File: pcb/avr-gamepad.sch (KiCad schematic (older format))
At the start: 64 parts, among them J1 Conn_01x06, J2 Conn_01x06, J3 Conn_01x05, J4 Conn_01x05, P1 USB_C_Plug_USB2.0, SW1 RESET, SW10 R2, SW11 A, SW13 Left, SW14 L2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

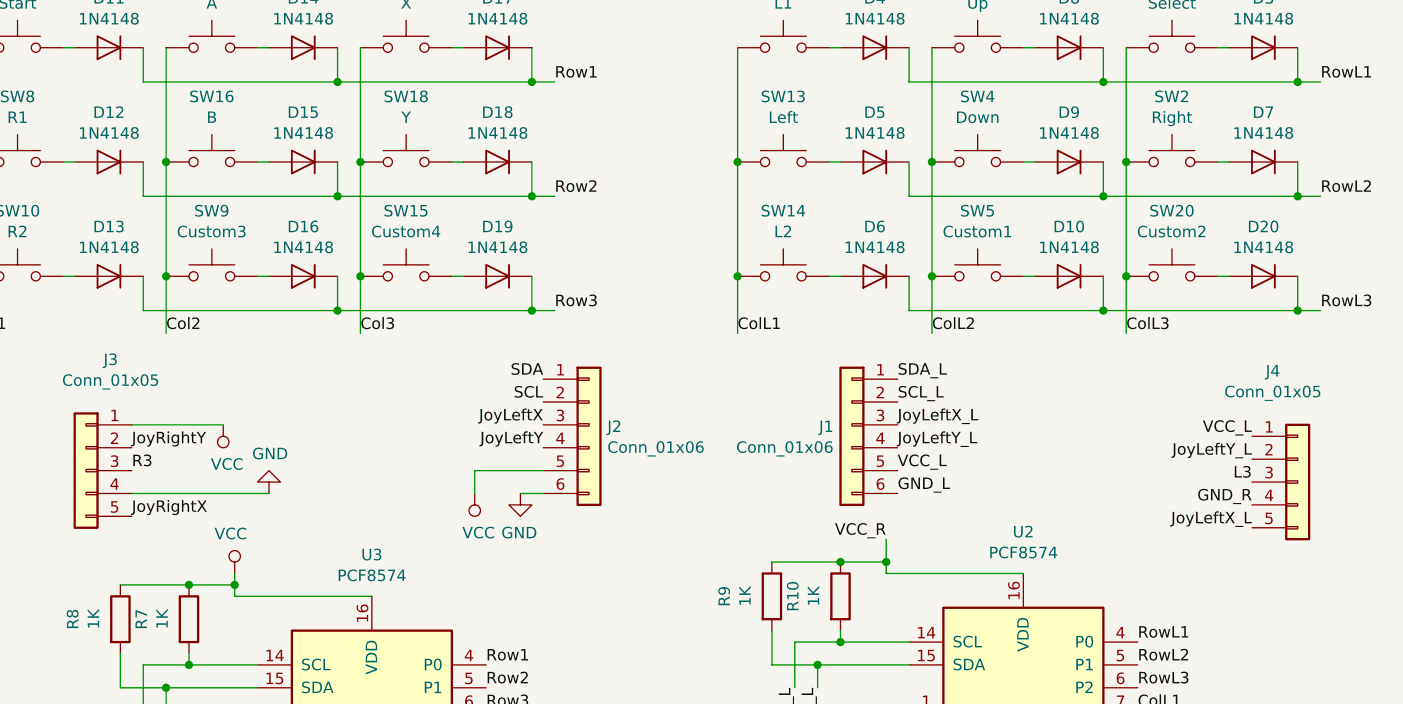
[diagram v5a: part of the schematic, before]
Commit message: disabled extra buttons, fixed R-L conversion
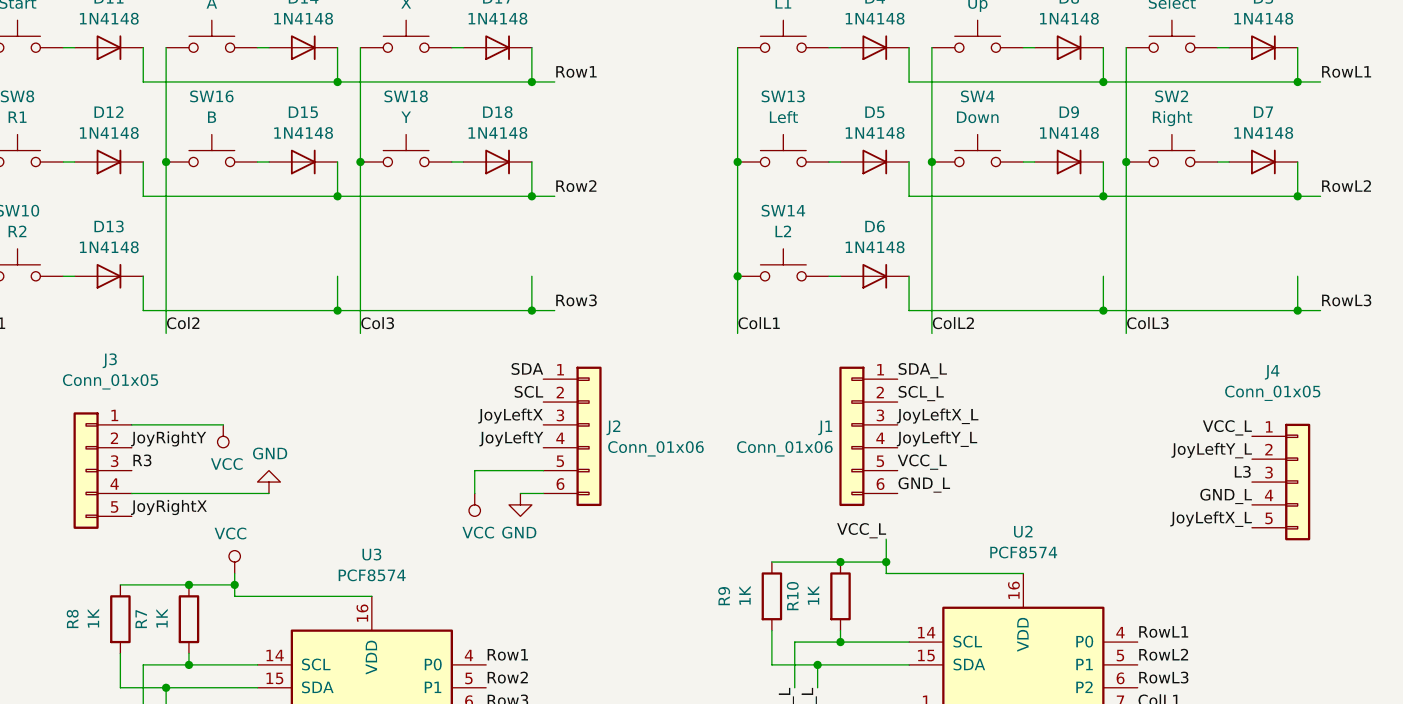
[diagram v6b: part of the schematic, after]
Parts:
- removed D10, D16, D19, D20: 1N4148, Diode_SMD:D_0603_1608Metric, symbol Diode:1N4148
- removed SW15: Custom4, button-contacts:Small, symbol Switch:SW_Push
- removed SW20: Custom2, button-contacts:Small, symbol Switch:SW_Push
- removed SW5: Custom1, button-contacts:Large_tapered, symbol Switch:SW_Push
- removed SW9: Custom3, button-contacts:Small, symbol Switch:SW_Push
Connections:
- net GND_R is gone; now on net GND_L: J4.4 (Pin_4)
- net VCC_R is gone; now on net VCC_L: R10.1, R9.1, U2.16 (VDD)
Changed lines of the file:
@@
 EESchema Schematic File Version 4
-LIBS:avr-gamepad-cache
-EELAYER 29 0
+EELAYER 30 0
 EELAYER END
 $Descr A4 11693 8268
@@
 GND_L
 Text Label 10500 2900 2    50   ~ 0
-GND_R
+GND_L
 Text Label 5600 2950 0    50   ~ 0
 JoyRightX
@@
 Wire Wire Line
 	8250 900  8250 1400
-Wire Wire Line
-	9100 1400 9100 1900
 Connection ~ 9100 1400
 Wire Wire Line
 	9100 900  9100 1400
-Wire Wire Line
-	9950 1400 9950 1900
 Connection ~ 9950 1400
 Wire Wire Line
 	9950 900  9950 1400
-$Comp
-L Switch:SW_Push SW20
-U 1 1 5F102509
-P 10150 1900
-F 0 "SW20" H 10150 2185 50  0000 C CNN
-F 1 "Custom2" H 10150 2094 50  0000 C CNN
-F 2 "button-contacts:Small" H 10150 2100 50  0001 C CNN
-F 3 "~" H 10150 2100 50  0001 C CNN
-	1    10150 1900
-	1    0    0    -1
-$EndComp
-$Comp
-L Diode:1N4148 D20
-U 1 1 5F1024F7
-P 10550 1900
-F 0 "D20" H 10550 1684 50  0000 C CNN
-F 1 "1N4148" H 10550 1775 50  0000 C CNN
-F 2 "Diode_SMD:D_0603_1608Metric" H 10550 1725 50  0001 C CNN
-F 3 "https://assets.nexperia.com/documents/data-sheet/1N4148_1N4448.pdf" H 10550 1900 50  0001 C CNN
-	1    10550 1900
-	-1   0    0    1
-$EndComp
-Wire Wire Line
-	10400 1900 10350 1900
 $Comp
 L Switch:SW_Push SW3
@@
 	-1   0    0    1
 $EndComp
-$Comp
-L Diode:1N4148 D10
-U 1 1 5EA4B7D9
-P 9700 1900
-F 0 "D10" H 9700 1684 50  0000 C CNN
-F 1 "1N4148" H 9700 1775 50  0000 C CNN
-F 2 "Diode_SMD:D_0603_1608Metric" H 9700 1725 50  0001 C CNN
-F 3 "https://assets.nexperia.com/documents/data-sheet/1N4148_1N4448.pdf" H 9700 1900 50  0001 C CNN
-	1    9700 1900
-	-1   0    0    1
-$EndComp
 Wire Wire Line
 	10400 1400 10350 1400
@@
 Wire Wire Line
 	9550 1400 9500 1400
-Wire Wire Line
-	9550 1900 9500 1900
 Text Label 10800 2050 0    50   ~ 0
 RowL3
@@
 Wire Wire Line
 	4900 900  4900 1400
-Wire Wire Line
-	5750 1400 5750 1900
 Connection ~ 5750 1400
-Connection ~ 5750 1900
 Wire Wire Line
 	5750 900  5750 1400
-Wire Wire Line
-	6600 1400 6600 1900
 Connection ~ 6600 1400
 Wire Wire Line
 	6600 900  6600 1400
-$Comp
-L Switch:SW_Push SW15
-U 1 1 5F40F877
-P 6800 1900
-F 0 "SW15" H 6800 2185 50  0000 C CNN
-F 1 "Custom4" H 6800 2094 50  0000 C CNN
-F 2 "button-contacts:Small" H 6800 2100 50  0001 C CNN
-F 3 "~" H 6800 2100 50  0001 C CNN
-	1    6800 1900
-	1    0    0    -1
-$EndComp
-$Comp
-L Diode:1N4148 D19
-U 1 1 5F40F87D
-P 7200 1900
-F 0 "D19" H 7200 1684 50  0000 C CNN
-F 1 "1N4148" H 7200 1775 50  0000 C CNN
-F 2 "Diode_SMD:D_0603_1608Metric" H 7200 1725 50  0001 C CNN
-F 3 "https://assets.nexperia.com/documents/data-sheet/1N4148_1N4448.pdf" H 7200 1900 50  0001 C CNN
-	1    7200 1900
-	-1   0    0    1
-$EndComp
-Wire Wire Line
-	7050 1900 7000 1900
 Text Label 6600 2150 0    50   ~ 0
 Col3
-Wire Wire Line
-	6600 1900 6600 2150
-Connection ~ 6600 1900
 $Comp
 L Switch:SW_Push SW11
@@
 	-1   0    0    1
 $EndComp
-$Comp
-L Diode:1N4148 D16
-U 1 1 5F40F8B1
-P 6350 1900
-F 0 "D16" H 6350 1684 50  0000 C CNN
-F 1 "1N4148" H 6350 1775 50  0000 C CNN
-F 2 "Diode_SMD:D_0603_1608Metric" H 6350 1725 50  0001 C CNN
-F 3 "https://assets.nexperia.com/documents/data-sheet/1N4148_1N4448.pdf" H 6350 1900 50  0001 C CNN
-	1    6350 1900
-	-1   0    0    1
-$EndComp
 Wire Wire Line
 	7050 1400 7000 1400
@@
 Wire Wire Line
 	6200 1400 6150 1400
-Wire Wire Line
-	6200 1900 6150 1900
 Text Label 5750 2150 0    50   ~ 0
 Col2
-Wire Wire Line
-	5750 1900 5750 2150
 Text Label 7450 2050 0    50   ~ 0
 Row3
@@
 ColL3
 Wire Wire Line
-	9950 1900 9950 2150
-Connection ~ 9950 1900
-Wire Wire Line
-	9100 1900 9100 2150
-Connection ~ 9100 1900
-Wire Wire Line
 	8250 1900 8250 2150
 Connection ~ 8250 1900
@@
 GND_L
 Text Label 8900 3050 2    50   ~ 0
-VCC_R
+VCC_L
 $Comp
 L power:GND #PWR0102
@@
 Text Label 7400 2650 2    50   ~ 0
 JoyLeftY
-$Comp
-L Switch:SW_Push SW5
-U 1 1 5CE3BF2C
-P 9300 1900
-F 0 "SW5" H 9300 2185 50  0000 C CNN
-F 1 "Custom1" H 9300 2094 50  0000 C CNN
-F 2 "button-contacts:Large_tapered" H 9300 2100 50  0001 C CNN
-F 3 "~" H 9300 2100 50  0001 C CNN
-	1    9300 1900
-	1    0    0    -1
-$EndComp
-$Comp
-L Switch:SW_Push SW9
-U 1 1 5F40F893
-P 5950 1900
-F 0 "SW9" H 5950 2185 50  0000 C CNN
-F 1 "Custom3" H 5950 2094 50  0000 C CNN
-F 2 "button-contacts:Small" H 5950 2100 50  0001 C CNN
-F 3 "~" H 5950 2100 50  0001 C CNN
-	1    5950 1900
-	1    0    0    -1
-$EndComp
+Wire Wire Line
+	6600 1400 6600 2150
+Wire Wire Line
+	5750 1400 5750 2150
+Wire Wire Line
+	9950 1400 9950 2150
+Wire Wire Line
+	9100 1400 9100 2150
 $EndSCHEMATC

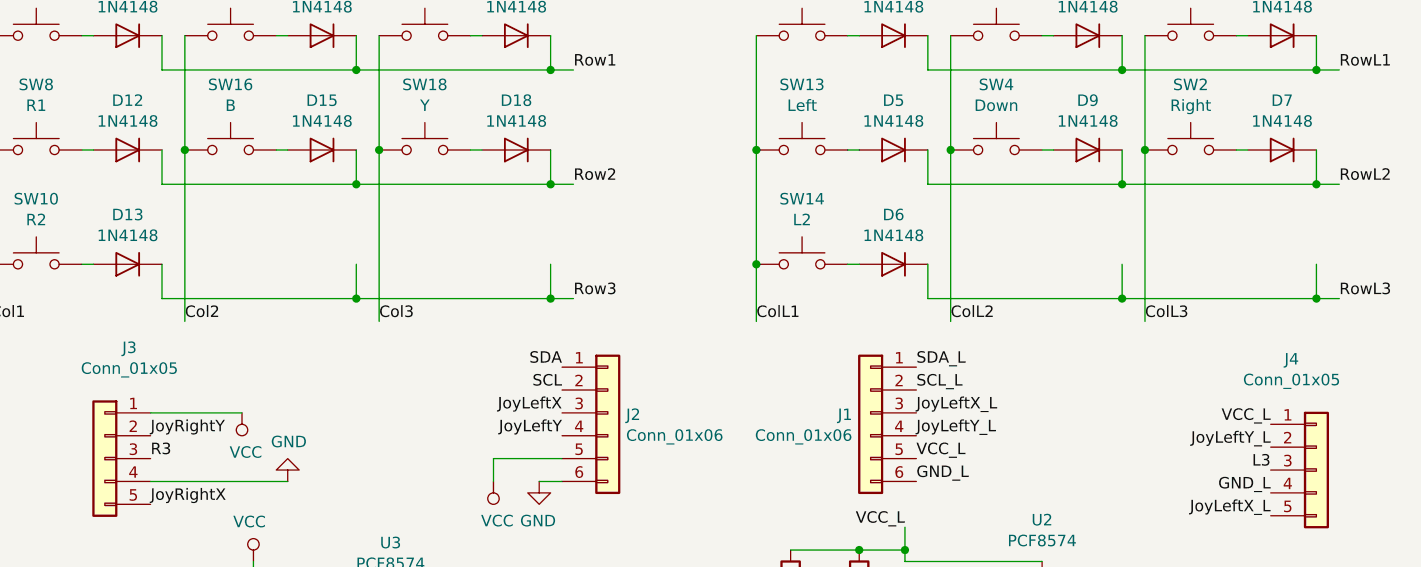
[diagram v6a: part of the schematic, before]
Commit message: swap left/right board sides for fab assembly
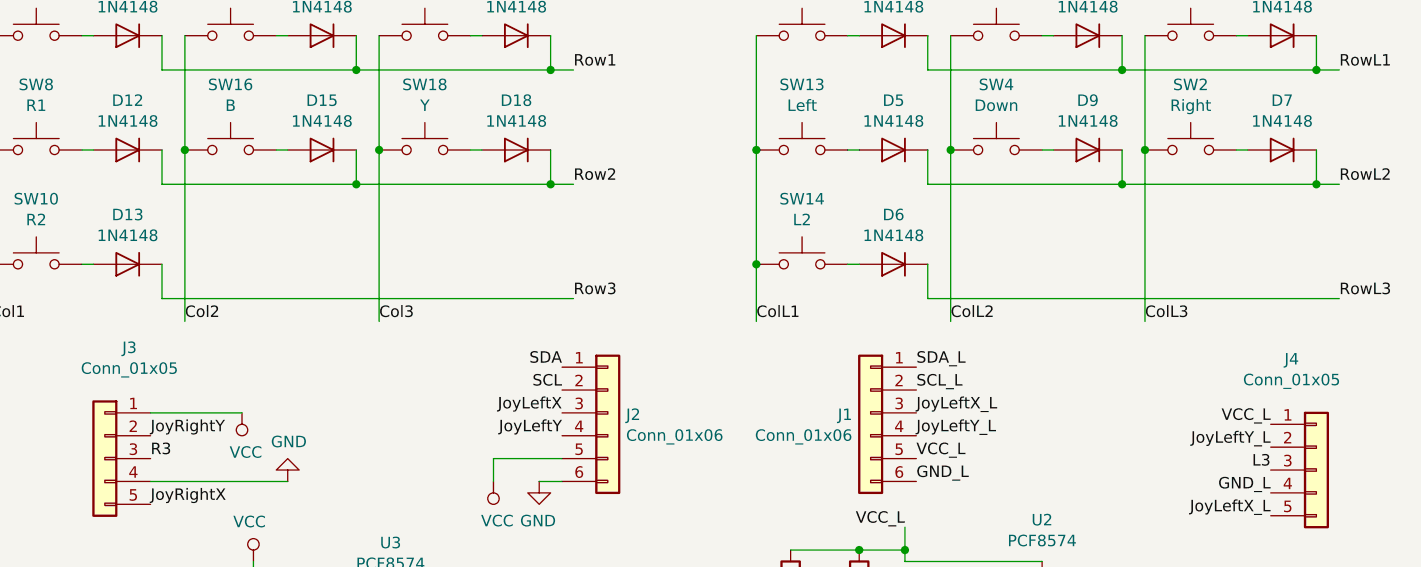
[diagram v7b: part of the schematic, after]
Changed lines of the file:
@@
 EESchema Schematic File Version 4
-EELAYER 30 0
+LIBS:avr-gamepad-cache
+EELAYER 29 0
 EELAYER END
 $Descr A4 11693 8268
@@
 	9000 1550 9000 1400
 Wire Wire Line
-	10800 2050 10700 2050
-Wire Wire Line
 	9000 2050 9000 1900
-Wire Wire Line
-	9850 1900 9850 2050
-Connection ~ 9850 2050
-Wire Wire Line
-	9850 2050 9000 2050
-Wire Wire Line
-	10700 1900 10700 2050
-Connection ~ 10700 2050
-Wire Wire Line
-	10700 2050 9850 2050
 Wire Wire Line
 	10700 1400 10700 1550
@@
 	5650 1550 5650 1400
 Wire Wire Line
-	7450 2050 7350 2050
-Wire Wire Line
 	5650 2050 5650 1900
-Wire Wire Line
-	6500 1900 6500 2050
-Connection ~ 6500 2050
-Wire Wire Line
-	6500 2050 5650 2050
-Wire Wire Line
-	7350 1900 7350 2050
-Connection ~ 7350 2050
-Wire Wire Line
-	7350 2050 6500 2050
 Wire Wire Line
 	7350 1400 7350 1550
@@
 Wire Wire Line
 	9100 1400 9100 2150
+Wire Wire Line
+	5650 2050 7450 2050
+Wire Wire Line
+	9000 2050 10800 2050
 $EndSCHEMATC

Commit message: pcb rearranging, placeholder footprint for right angle tact switches
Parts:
- J1, J2: footprint Connector_FFC-FPC:Hirose_FH12-8S-0.5SH_1x08-1MP_P0.50mm_Horizontal -> Connector_FFC-FPC:Hirose_FH12-6S-0.5SH_1x06-1MP_P0.50mm_Horizontal
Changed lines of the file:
@@
 F 0 "J1" H 8830 2542 50  0000 L CNN
 F 1 "Conn_01x06" H 8830 2451 50  0000 L CNN
-F 2 "Connector_FFC-FPC:Hirose_FH12-8S-0.5SH_1x08-1MP_P0.50mm_Horizontal" H 8750 2550 50  0001 C CNN
+F 2 "Connector_FFC-FPC:Hirose_FH12-6S-0.5SH_1x06-1MP_P0.50mm_Horizontal" H 8750 2550 50  0001 C CNN
 F 3 "~" H 8750 2550 50  0001 C CNN
 	1    8750 2550
@@
 F 0 "J2" H 7680 2542 50  0000 L CNN
 F 1 "Conn_01x06" H 7680 2451 50  0000 L CNN
-F 2 "Connector_FFC-FPC:Hirose_FH12-8S-0.5SH_1x08-1MP_P0.50mm_Horizontal" H 7600 2550 50  0001 C CNN
+F 2 "Connector_FFC-FPC:Hirose_FH12-6S-0.5SH_1x06-1MP_P0.50mm_Horizontal" H 7600 2550 50  0001 C CNN
 F 3 "~" H 7600 2550 50  0001 C CNN
 	1    7600 2550
